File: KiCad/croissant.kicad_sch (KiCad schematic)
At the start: 51 parts, among them J1 USB_C_Receptacle_PowerOnly_6P, Q1 NMOS, SW1 SW_SPST, U1 NE556, U2 TL064

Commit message: Add footprints
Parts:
- C1, C2, C3, C4, C5, C6, C7: footprint (none) -> Capacitor_SMD:C_0603_1608Metric
- D1, D10, D11, D12, D13, D14, D15, D2, D3, D4, D5, D6, D7, D8, D9, J1, Q1, R1, R2, R3: footprint (none) -> LED_SMD:LED_0603_1608Metric
- R10, R11, R12, R13, R14, R15, R16, R17, R18, R19, R20, R21, R22, R23, R24, R4, R5, R6, R7, R8, R9: footprint (none) -> Resistor_SMD:R_0603_1608Metric
- U2: footprint (none) -> Package_SO:SOIC-14_3.9x8.7mm_P1.27mm

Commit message: Fix ERC
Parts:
- added R25: 0, Resistor_SMD:R_0603_1608Metric, symbol Device:R
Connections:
- net +5V: now also R25.1; no longer Q1.1 (D), R10.1, R11.1, R12.1, R13.1, R14.1, R15.1, R16.1, R17.1, R18.1, R19.1, R20.1, R21.1, R22.1, R23.1, R24.1, R9.1
- new net PWMOut: Q1.1 (D), R10.1, R11.1, R12.1, R13.1, R14.1, R15.1, R16.1, R17.1, R18.1, R19.1, R20.1, R21.1, R22.1, R23.1, R24.1, R25.2, R9.1
- no-connect marks 4 -> 6
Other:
- moved on the sheet: C4, C5, C7, Q1, R24, R5, U1B

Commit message: Fix footprints
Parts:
- J1: footprint LED_SMD:LED_0603_1608Metric -> Connector_USB:USB_C_Receptacle_GCT_USB4135-GF-A_6P_TopMnt_Horizontal
- Q1: footprint LED_SMD:LED_0603_1608Metric -> Package_TO_SOT_SMD:SOT-23
- R1, R2, R3: footprint LED_SMD:LED_0603_1608Metric -> Resistor_SMD:R_0603_1608Metric
- SW1: footprint (none) -> Package_TO_SOT_SMD:SOT-23
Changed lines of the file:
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@@
       (effects (font (size 1.27 1.27)) (justify left))
     )
-    (property "Footprint" "LED_SMD:LED_0603_1608Metric" (at 264.16 129.54 0)
+    (property "Footprint" "Package_TO_SOT_SMD:SOT-23" (at 264.16 129.54 0)
       (effects (font (size 1.27 1.27)) hide)
     )
@@
       (effects (font (size 1.27 1.27)) (justify left))
     )
-    (property "Footprint" "LED_SMD:LED_0603_1608Metric" (at 107.442 58.42 90)
+    (property "Footprint" "Resistor_SMD:R_0603_1608Metric" (at 107.442 58.42 90)
       (effects (font (size 1.27 1.27)) hide)
     )
@@
       (effects (font (size 1.27 1.27)))
     )
-    (property "Footprint" "" (at 60.96 55.88 0)
+    (property "Footprint" "Package_TO_SOT_SMD:SOT-23" (at 60.96 55.88 0)
       (effects (font (size 1.27 1.27)) hide)
     )
@@
       (effects (font (size 1.27 1.27)) (justify left))
     )
-    (property "Footprint" "LED_SMD:LED_0603_1608Metric" (at 61.722 135.89 90)
+    (property "Footprint" "Resistor_SMD:R_0603_1608Metric" (at 61.722 135.89 90)
       (effects (font (size 1.27 1.27)) hide)
     )
@@
       (effects (font (size 1.27 1.27)))
     )
-    (property "Footprint" "LED_SMD:LED_0603_1608Metric" (at 69.85 133.858 90)
+    (property "Footprint" "Resistor_SMD:R_0603_1608Metric" (at 69.85 133.858 90)
       (effects (font (size 1.27 1.27)) hide)
     )
@@
       (effects (font (size 1.27 1.27)))
     )
-    (property "Footprint" "LED_SMD:LED_0603_1608Metric" (at 44.45 60.96 0)
-      (effects (font (size 1.27 1.27)) hide)
-    )
+    (property "Footprint" "Connector_USB:USB_C_Receptacle_GCT_USB4135-GF-A_6P_TopMnt_Horizontal" (at 44.45 60.96 0)
+      (effects (font (size 1.27 1.27)) hide)
+    )

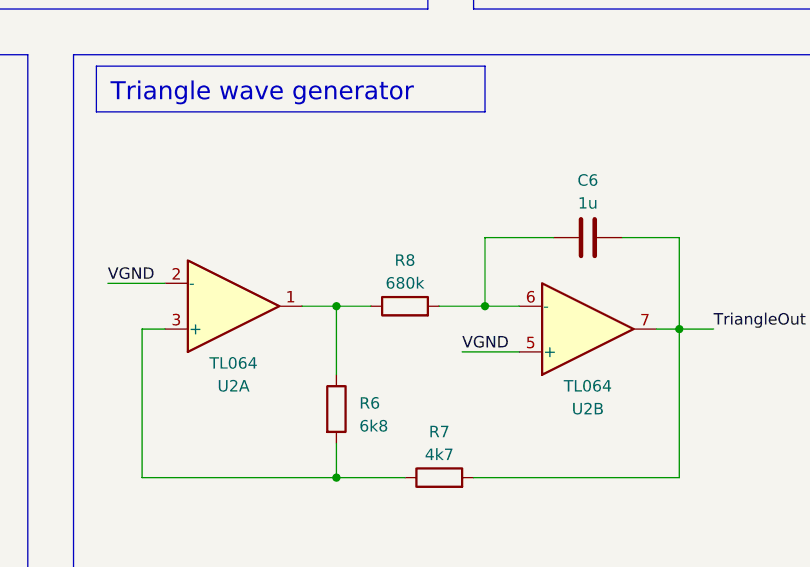
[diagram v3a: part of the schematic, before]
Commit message: Lower frequency
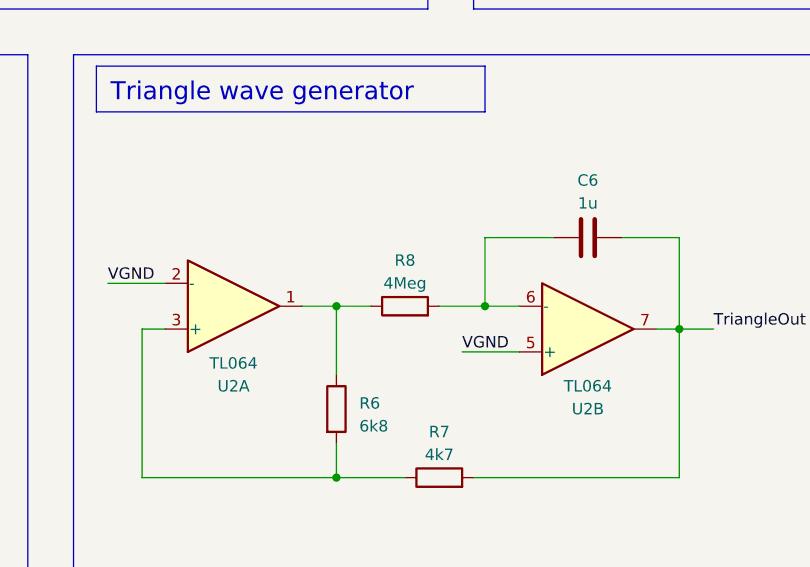
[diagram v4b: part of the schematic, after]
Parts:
- R8: value 680k -> 4Meg
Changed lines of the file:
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@@
       (effects (font (size 1.27 1.27)))
     )
-    (property "Value" "680k" (at 143.51 121.92 90)
+    (property "Value" "4Meg" (at 143.51 121.92 90)
       (effects (font (size 1.27 1.27)))
     )

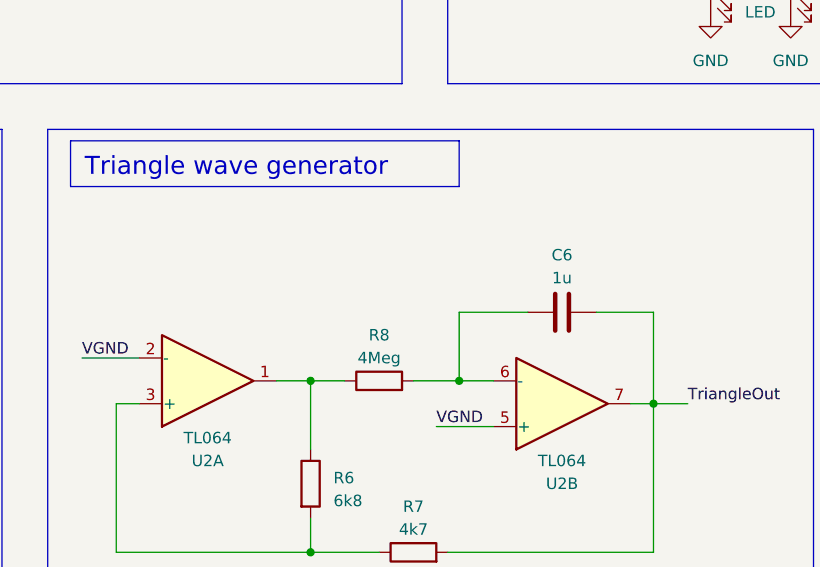
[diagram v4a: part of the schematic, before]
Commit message: Add second cap footprint
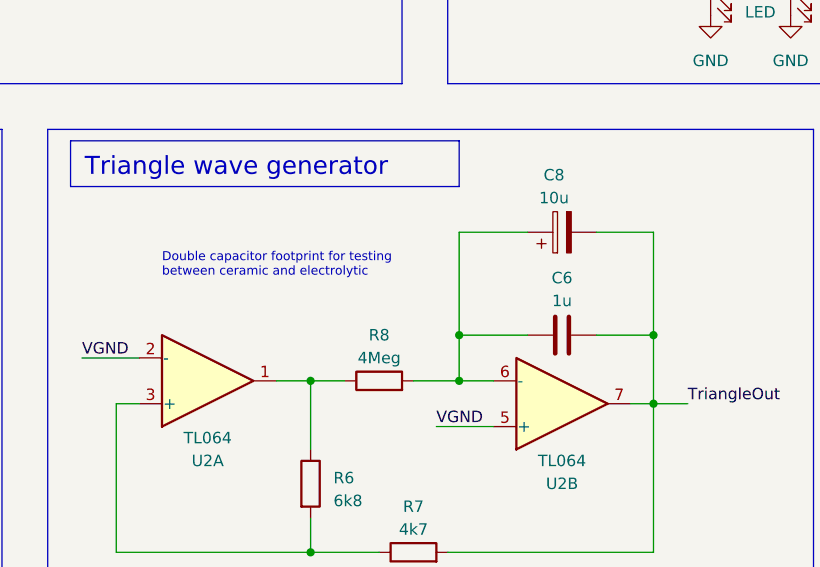
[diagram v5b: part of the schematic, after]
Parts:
- added C8: 10u, symbol Device:C_Polarized
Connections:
- net TriangleOut: now also C8.2
- net at C6.1, R8.2, U2.6 (-): now also C8.1
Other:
- note added: "Double capacitor footprint for testing between ceramic and electrolytic"
- moved on the sheet: C6
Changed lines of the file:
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@@
   (junction (at 152.4 124.46) (diameter 0) (color 0 0 0 0)
   )
+  (junction (at 173.99 119.38) (diameter 0) (color 0 0 0 0)
+  )
   (junction (at 173.99 127) (diameter 0) (color 0 0 0 0)
   )
@@
   )
   (junction (at 207.01 68.58) (diameter 0) (color 0 0 0 0)
+  )
+  (junction (at 152.4 119.38) (diameter 0) (color 0 0 0 0)
   )
   (junction (at 45.72 113.03) (diameter 0) (color 0 0 0 0)
@@
   (no_connect (at 55.88 68.58))
   (no_connect (at 55.88 71.12))
+  (wire (pts (xy 160.02 107.95) (xy 152.4 107.95))
+    (stroke (width 0) (type default))
+  )
   (wire (pts (xy 133.35 72.39) (xy 133.35 66.04))
     (stroke (width 0) (type default))
@@
     (stroke (width 0) (type default))
   )
+  (wire (pts (xy 167.64 107.95) (xy 173.99 107.95))
+    (stroke (width 0) (type default))
+  )
   (wire (pts (xy 45.72 113.03) (xy 45.72 121.92))
     (stroke (width 0) (type default))
@@
     (stroke (width 0) (type default))
   )
-  (wire (pts (xy 152.4 116.84) (xy 152.4 124.46))
+  (wire (pts (xy 152.4 119.38) (xy 152.4 124.46))
     (stroke (width 0) (type default))
   )
@@
     (stroke (width 0) (type default))
   )
+  (wire (pts (xy 173.99 107.95) (xy 173.99 119.38))
+    (stroke (width 0) (type default))
+  )
   (wire (pts (xy 40.64 83.82) (xy 40.64 82.55))
     (stroke (width 0) (type default))
@@
     (stroke (width 0) (type default))
   )
-  (wire (pts (xy 160.02 116.84) (xy 152.4 116.84))
-    (stroke (width 0) (type default))
-  )
-  (wire (pts (xy 167.64 116.84) (xy 173.99 116.84))
+  (wire (pts (xy 160.02 119.38) (xy 152.4 119.38))
+    (stroke (width 0) (type default))
+  )
+  (wire (pts (xy 167.64 119.38) (xy 173.99 119.38))
     (stroke (width 0) (type default))
   )
@@
     (stroke (width 0) (type default))
   )
-  (wire (pts (xy 173.99 116.84) (xy 173.99 127))
+  (wire (pts (xy 173.99 119.38) (xy 173.99 127))
     (stroke (width 0) (type default))
   )
   (wire (pts (xy 63.5 132.08) (xy 66.04 132.08))
+    (stroke (width 0) (type default))
+  )
+  (wire (pts (xy 152.4 107.95) (xy 152.4 119.38))
     (stroke (width 0) (type default))
   )
@@
     (fill (type none))
     (effects (font (size 2 2)) (justify left top))
+  )
+  (text "Double capacitor footprint for testing\nbetween ceramic and electrolytic"
+    (at 119.38 113.03 0)
+    (effects (font (size 1 1)) (justify left bottom))
   )
   (label "PWMOut" (at 163.83 44.45 0) (fields_autoplaced)
@@
     )
   )
-  (symbol (lib_id "Device:C") (at 163.83 116.84 90) (unit 1)
-    (in_bom yes) (on_board yes) (dnp no) (fields_autoplaced)
-    (property "Reference" "C6" (at 163.83 110.49 90)
-      (effects (font (size 1.27 1.27)))
-    )
-    (property "Value" "1u" (at 163.83 113.03 90)
-      (effects (font (size 1.27 1.27)))
-    )
-    (property "Footprint" "Capacitor_SMD:C_0603_1608Metric" (at 167.64 115.8748 0)
-      (effects (font (size 1.27 1.27)) hide)
-    )
-    (property "Datasheet" "~" (at 163.83 116.84 0)
+  (symbol (lib_id "Device:C") (at 163.83 119.38 90) (unit 1)
+    (in_bom yes) (on_board yes) (dnp no) (fields_autoplaced)
+    (property "Reference" "C6" (at 163.83 113.03 90)
+      (effects (font (size 1.27 1.27)))
+    )
+    (property "Value" "1u" (at 163.83 115.57 90)
+      (effects (font (size 1.27 1.27)))
+    )
+    (property "Footprint" "Capacitor_SMD:C_0603_1608Metric" (at 167.64 118.4148 0)
+      (effects (font (size 1.27 1.27)) hide)
+    )
+    (property "Datasheet" "~" (at 163.83 119.38 0)
       (effects (font (size 1.27 1.27)) hide)
     )
@@
         )
       )
+    )
+  )
+  (symbol (lib_id "Device:C_Polarized") (at 163.83 107.95 90) (unit 1)
+    (in_bom yes) (on_board yes) (dnp no) (fields_autoplaced)
+    (property "Reference" "C8" (at 162.941 101.6 90)
+      (effects (font (size 1.27 1.27)))
+    )
+    (property "Value" "10u" (at 162.941 104.14 90)
+      (effects (font (size 1.27 1.27)))
+    )
+    (property "Footprint" "" (at 167.64 106.9848 0)
+      (effects (font (size 1.27 1.27)) hide)
+    )
+    (property "Datasheet" "~" (at 163.83 107.95 0)
+      (effects (font (size 1.27 1.27)) hide)
+    )
+    (pin "1")
+    (pin "2")
+    (instances
+      (project "croissant"
+        (path "/9d4c4425-9345-4751-a711-72e95f2cc96d"
+          (reference "C8") (unit 1)
+        )
+      )

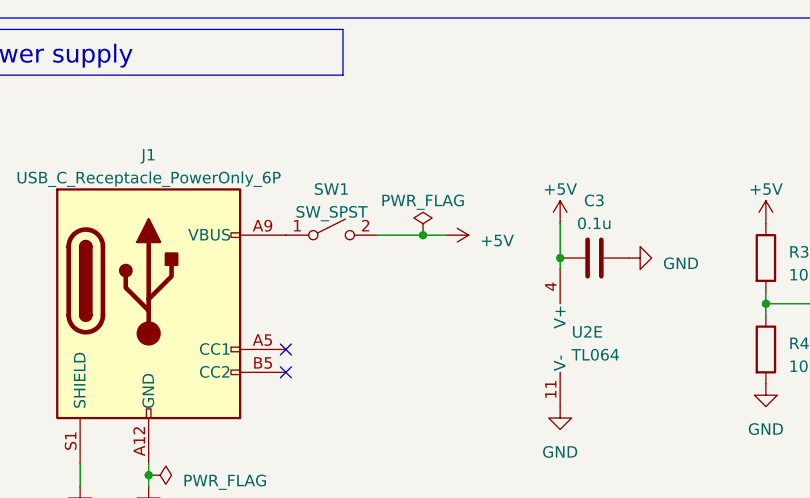
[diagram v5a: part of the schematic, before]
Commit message: Change SPST to SPDT
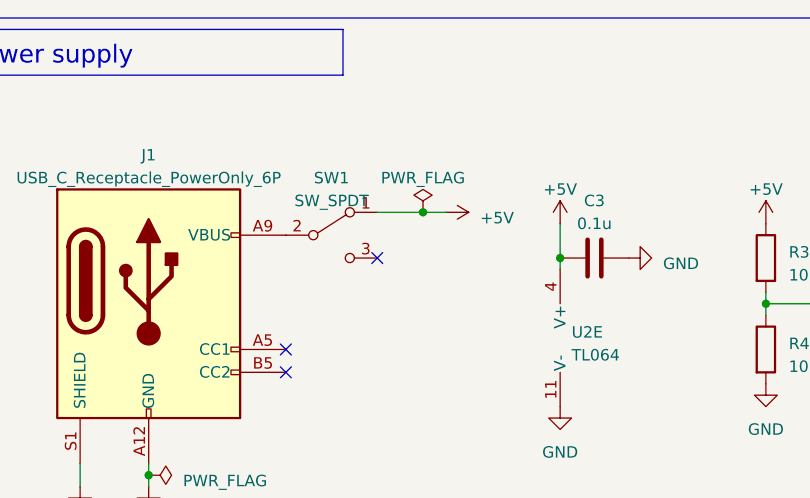
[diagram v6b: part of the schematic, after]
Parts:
- removed SW1: SW_SPST, Package_TO_SOT_SMD:SOT-23, symbol Switch:SW_SPST
- added SW1: SW_SPDT, symbol Switch:SW_SPDT
- C8: footprint (none) -> Capacitor_SMD:CP_Elec_4x3
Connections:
- net +5V: now also SW1.1 (A)
- net at J1.A9 (VBUS), J1.B9 (VBUS): now also SW1.2 (B)
- no-connect marks 6 -> 7
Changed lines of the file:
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@@
   (junction (at 238.76 142.24) (diameter 0) (color 0 0 0 0)
   )
-  (junction (at 71.12 55.88) (diameter 0) (color 0 0 0 0)
+  (junction (at 71.12 53.34) (diameter 0) (color 0 0 0 0)
   )
   (junction (at 250.19 132.08) (diameter 0) (color 0 0 0 0)
@@
   (no_connect (at 118.11 40.64))
   (no_connect (at 118.11 45.72))
+  (no_connect (at 66.04 58.42))
   (no_connect (at 55.88 68.58))
   (no_connect (at 55.88 71.12))
@@
     (stroke (width 0) (type default))
   )
-  (wire (pts (xy 73.66 55.88) (xy 71.12 55.88))
+  (wire (pts (xy 73.66 53.34) (xy 71.12 53.34))
     (stroke (width 0) (type default))
   )
@@
     (stroke (width 0) (type default))
   )
-  (wire (pts (xy 71.12 55.88) (xy 66.04 55.88))
+  (wire (pts (xy 71.12 53.34) (xy 66.04 53.34))
     (stroke (width 0) (type default))
   )
@@
     )
   )
-  (symbol (lib_id "Switch:SW_SPST") (at 60.96 55.88 0) (unit 1)
-    (in_bom yes) (on_board yes) (dnp no) (fields_autoplaced)
-    (property "Reference" "SW1" (at 60.96 50.8 0)
-      (effects (font (size 1.27 1.27)))
-    )
-    (property "Value" "SW_SPST" (at 60.96 53.34 0)
-      (effects (font (size 1.27 1.27)))
-    )
-    (property "Footprint" "Package_TO_SOT_SMD:SOT-23" (at 60.96 55.88 0)
-      (effects (font (size 1.27 1.27)) hide)
-    )
-    (property "Datasheet" "~" (at 60.96 55.88 0)
-      (effects (font (size 1.27 1.27)) hide)
-    )
-    (pin "1")
-    (pin "2")
-    (instances
-      (project "croissant"
-        (path "/9d4c4425-9345-4751-a711-72e95f2cc96d"
-          (reference "SW1") (unit 1)
-        )
-      )
-    )
-  )
   (symbol (lib_id "power:GND") (at 224.79 83.82 0) (unit 1)
     (in_bom yes) (on_board yes) (dnp no) (fields_autoplaced)
@@
       (effects (font (size 1.27 1.27)))
     )
-    (property "Footprint" "" (at 167.64 106.9848 0)
+    (property "Footprint" "Capacitor_SMD:CP_Elec_4x3" (at 167.64 106.9848 0)
       (effects (font (size 1.27 1.27)) hide)
     )
@@
     )
   )
-  (symbol (lib_id "power:PWR_FLAG") (at 71.12 55.88 0) (unit 1)
-    (in_bom yes) (on_board yes) (dnp no) (fields_autoplaced)
-    (property "Reference" "#FLG01" (at 71.12 53.975 0)
-      (effects (font (size 1.27 1.27)) hide)
-    )
-    (property "Value" "PWR_FLAG" (at 71.12 52.07 0)
-      (effects (font (size 1.27 1.27)))
-    )
-    (property "Footprint" "" (at 71.12 55.88 0)
-      (effects (font (size 1.27 1.27)) hide)
-    )
-    (property "Datasheet" "~" (at 71.12 55.88 0)
+  (symbol (lib_id "power:PWR_FLAG") (at 71.12 53.34 0) (unit 1)
+    (in_bom yes) (on_board yes) (dnp no) (fields_autoplaced)
+    (property "Reference" "#FLG01" (at 71.12 51.435 0)
+      (effects (font (size 1.27 1.27)) hide)
+    )
+    (property "Value" "PWR_FLAG" (at 71.12 49.53 0)
+      (effects (font (size 1.27 1.27)))
+    )
+    (property "Footprint" "" (at 71.12 53.34 0)
+      (effects (font (size 1.27 1.27)) hide)
+    )
+    (property "Datasheet" "~" (at 71.12 53.34 0)
       (effects (font (size 1.27 1.27)) hide)
     )
@@
     )
   )
-  (symbol (lib_id "power:+5V") (at 73.66 55.88 270) (unit 1)
-    (in_bom yes) (on_board yes) (dnp no) (fields_autoplaced)
-    (property "Reference" "#PWR07" (at 69.85 55.88 0)
-      (effects (font (size 1.27 1.27)) hide)
-    )
-    (property "Value" "+5V" (at 77.47 56.515 90)
-      (effects (font (size 1.27 1.27)) (justify left))
-    )
-    (property "Footprint" "" (at 73.66 55.88 0)
-      (effects (font (size 1.27 1.27)) hide)
-    )
-    (property "Datasheet" "" (at 73.66 55.88 0)
+  (symbol (lib_id "power:+5V") (at 73.66 53.34 270) (unit 1)
+    (in_bom yes) (on_board yes) (dnp no) (fields_autoplaced)
+    (property "Reference" "#PWR07" (at 69.85 53.34 0)
+      (effects (font (size 1.27 1.27)) hide)
+    )
+    (property "Value" "+5V" (at 77.47 53.975 90)
+      (effects (font (size 1.27 1.27)) (justify left))
+    )
+    (property "Footprint" "" (at 73.66 53.34 0)
+      (effects (font (size 1.27 1.27)) hide)
+    )
+    (property "Datasheet" "" (at 73.66 53.34 0)
       (effects (font (size 1.27 1.27)) hide)
     )
@@
         )
       )
+    )
+  )
+  (symbol (lib_id "Switch:SW_SPDT") (at 60.96 55.88 0) (unit 1)
+    (in_bom yes) (on_board yes) (dnp no) (fields_autoplaced)
+    (property "Reference" "SW1" (at 60.96 49.53 0)
+      (effects (font (size 1.27 1.27)))
+    )
+    (property "Value" "SW_SPDT" (at 60.96 52.07 0)
+      (effects (font (size 1.27 1.27)))
+    )
+    (property "Footprint" "" (at 60.96 55.88 0)
+      (effects (font (size 1.27 1.27)) hide)
+    )
+    (property "Datasheet" "~" (at 60.96 55.88 0)
+      (effects (font (size 1.27 1.27)) hide)
+    )
+    (pin "1")
+    (pin "2")
+    (pin "3")
+    (instances
+      (project "croissant"
+        (path "/9d4c4425-9345-4751-a711-72e95f2cc96d"
+          (reference "SW1") (unit 1)
+        )
+      )

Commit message: Add SPDT footprint
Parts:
- SW1: footprint (none) -> croissant:JS102011JCQN
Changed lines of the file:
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@@
       (effects (font (size 1.27 1.27)))
     )
-    (property "Footprint" "" (at 60.96 55.88 0)
+    (property "Footprint" "croissant:JS102011JCQN" (at 60.96 55.88 0)
       (effects (font (size 1.27 1.27)) hide)
     )
